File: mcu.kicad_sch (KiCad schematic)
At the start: 45 parts, among them J201 DISP, J202 SWD, J203 SPI, J204 USB serial, Q201 2N7002, SW201 Reset, U201 STM32F103CBT6, U202 USBLC6-2SC6, U203 AMS1117-3.3, Y201 8MHz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

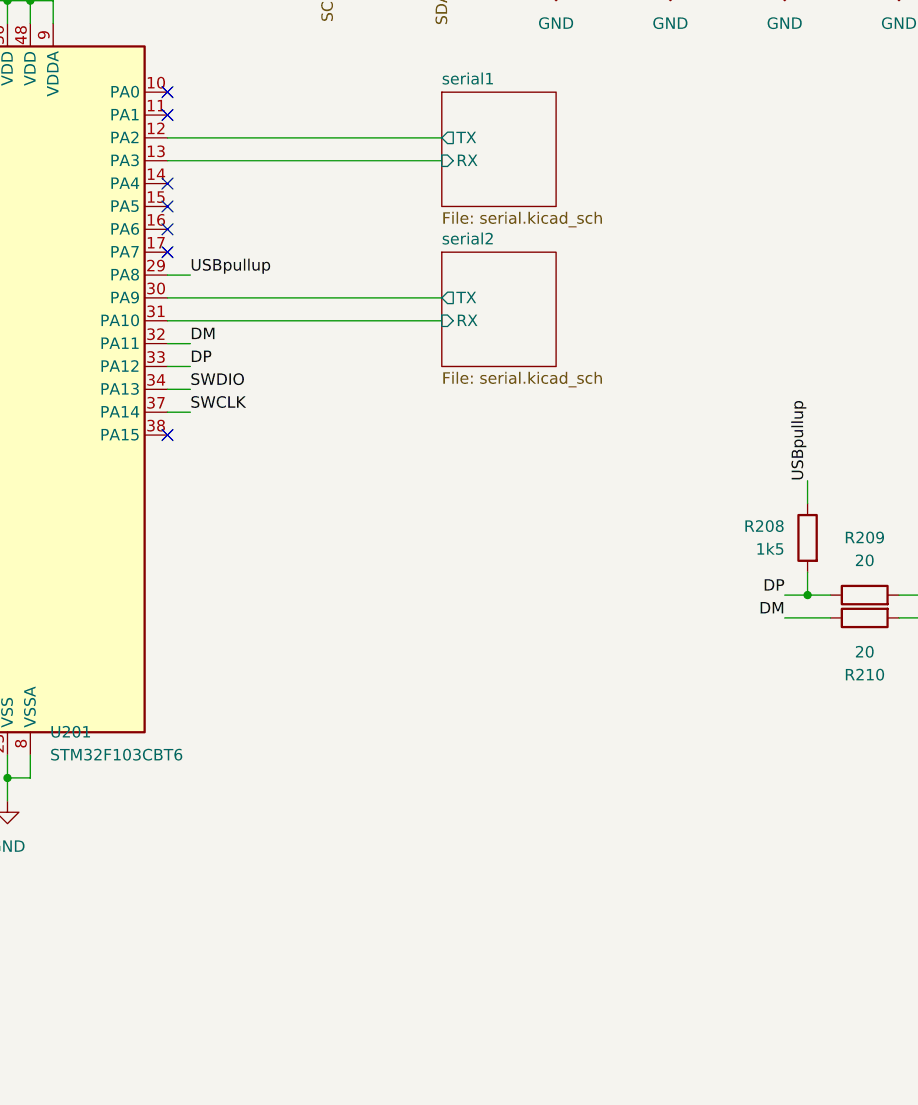
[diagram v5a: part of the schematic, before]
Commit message: Add MCU LEDs
Signed-off-by: Benedikt Spranger <b.spranger@linutronix.de>
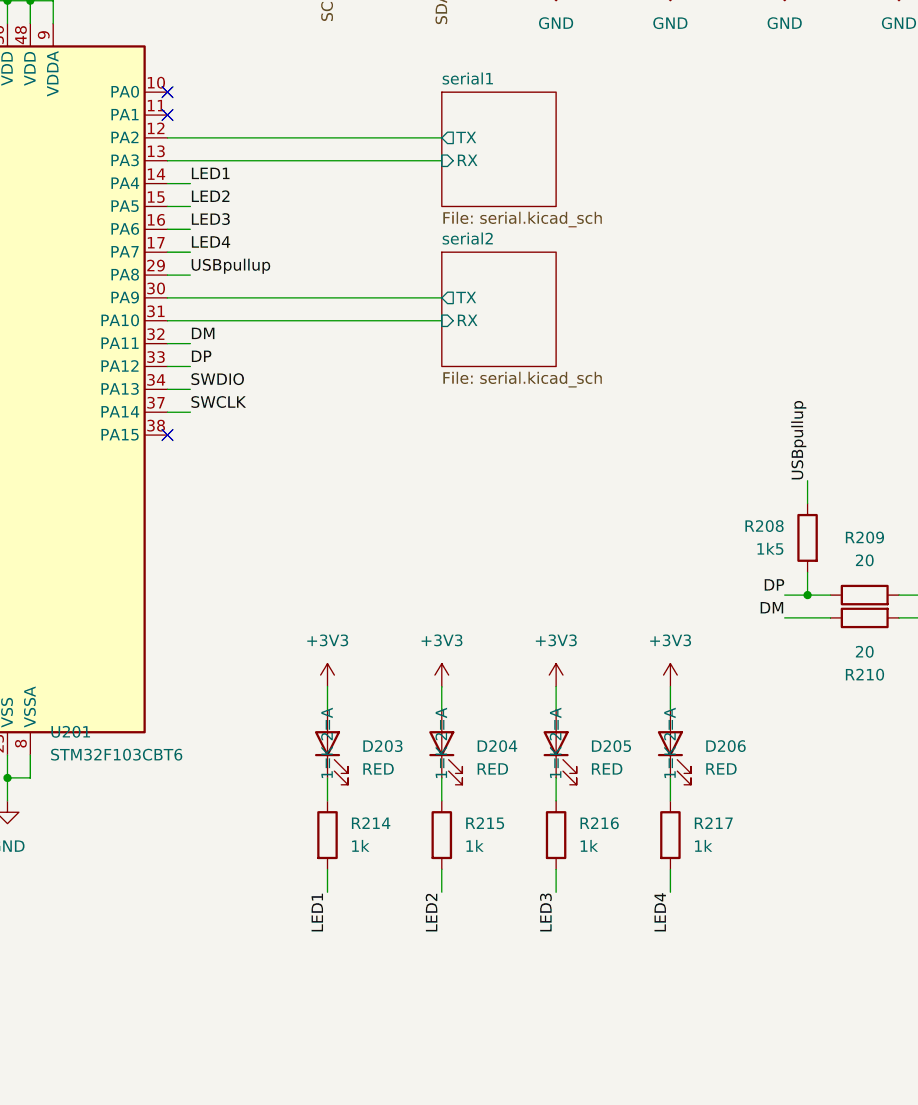
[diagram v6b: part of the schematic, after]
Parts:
- added D203, D204, D205, D206: RED, LED_SMD:LED_0603_1608Metric, symbol Device:LED
- added R214, R215, R216, R217: 1k, Resistor_SMD:R_0402_1005Metric, symbol Device:R
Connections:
- net +3V3: now also D203.2 (A), D204.2 (A), D205.2 (A), D206.2 (A)
- net LED1: now reaches U201.14 (PA4)
- net LED1: now also R214.2
- net LED2: now reaches U201.15 (PA5)
- net LED2: now also R215.2
- net LED3: now reaches U201.16 (PA6)
- net LED3: now also R216.2
- net LED4: now reaches U201.17 (PA7)
- net LED4: now also R217.2
- new net: D204.1 (K), R215.1
- new net: D205.1 (K), R216.1
- new net: D203.1 (K), R214.1
- new net: D206.1 (K), R217.1
- no-connect marks 13 -> 9

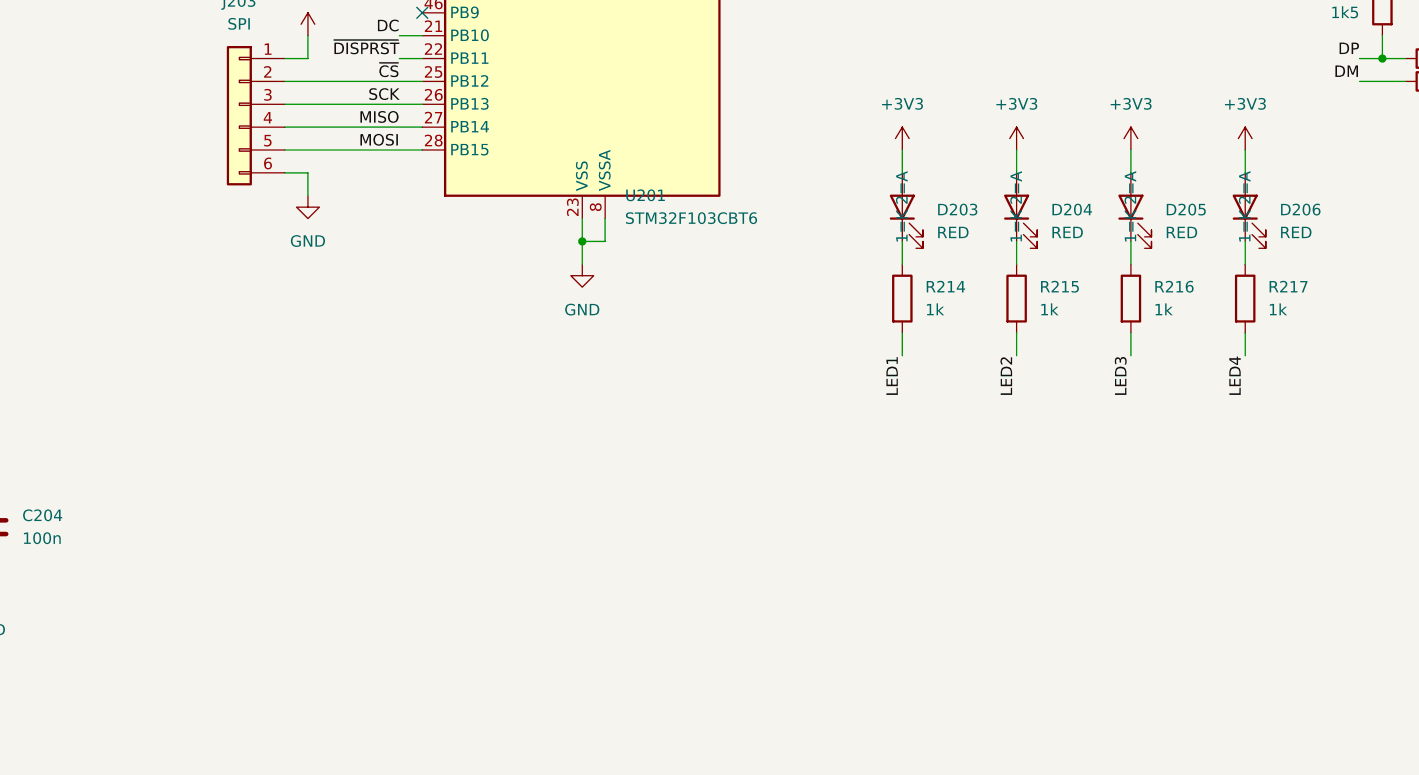
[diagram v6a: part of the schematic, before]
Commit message: Enable external I2C programming
Signed-off-by: Benedikt Spranger <b.spranger@linutronix.de>
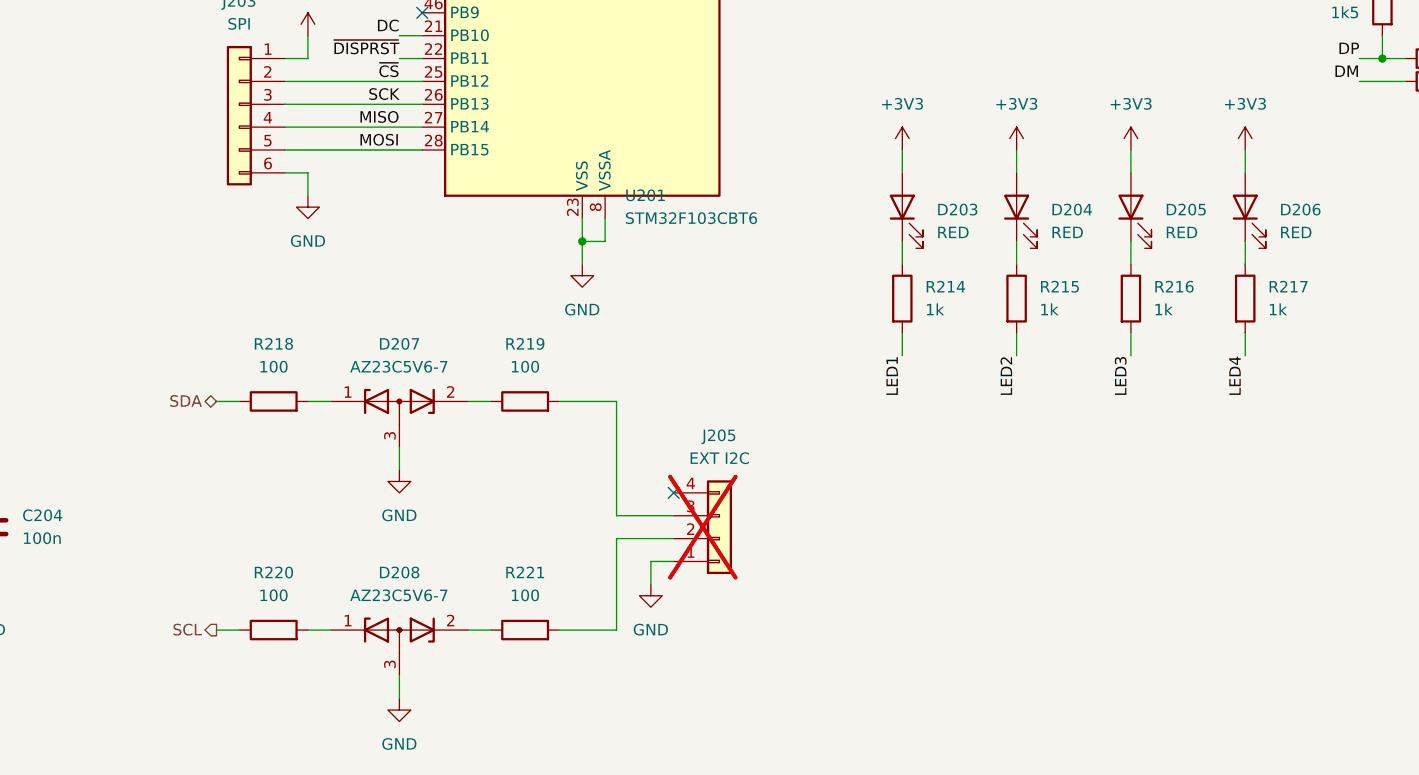
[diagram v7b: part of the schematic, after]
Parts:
- added D207, D208: AZ23C5V6-7, Package_TO_SOT_SMD:SOT-23, symbol Device:D_Zener_Dual_CommonAnode_KKA
- added J205: EXT I2C, Connector_Molex:Molex_KK-254_AE-6410-04A_1x04_P2.54mm_Vertical, symbol Connector_Generic:Conn_01x04
- added R218, R219, R220, R221: 100, Resistor_SMD:R_0402_1005Metric, symbol Device:R
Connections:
- net GND: now also D207.3 (A), D208.3 (A), J205.1 (Pin_1)
- net SCL: now also R220.1
- net SDA: now also R218.1
- new net: D207.2 (K), R219.1
- new net: J205.3 (Pin_3), R219.2
- new net: D208.1 (K), R220.2
- new net: D208.2 (K), R221.1
- new net: J205.2 (Pin_2), R221.2
- new net: D207.1 (K), R218.2
- no-connect marks 9 -> 10

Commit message: Available Parts
Signed-off-by: Benedikt Spranger <bene@eurovibes.org>
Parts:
- D203, D204, D205, D206: Long Description 90mcd Red 615nm~630nm Upright, surface-mount Red 120° 75mW 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 -> -40℃~+85℃ Red 0603 LED Indication - Discrete ROHS; MF XINGLIGHT -> Hubei KENTO Elec; MP XL-1608VRC-06 -> KT-0603R; SupplLink https://jlcpcb.com/partdetail/Xinglight-XL_1608VRC06/C73719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 -> https://jlcpcb.com/partdetail/Hubei_KentoElec-KT0603R/C2286; lcsc# C7371906 -> C2286
- R202, R204, R212: Long Description 62.5mW Thick Film Resistors 50V ±100ppm/℃ ±1% 4.7kΩ 0402 Ch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 -> 62.5mW Thick Film Resistors 50V ±100ppm/℃ ±1% 1MΩ 0402 Chip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; MP 0402WGF4701TCE -> 0402WGF1004TCE; SupplLink https://jlcpcb.com/partdetail/26643-0402WGF4701TCE/C25900 -> https://jlcpcb.com/partdetail/26826-0402WGF1004TCE/C26083; lcsc# C25900 -> C26083
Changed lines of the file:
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@@
 			)
 		)
-		(property "lcsc#" "C7371906"
+		(property "lcsc#" "C2286"
 			(at 165.1 135.89 0)
 			(effects
@@
 			)
 		)
-		(property "Long Description" "90mcd Red 615nm~630nm Upright, surface-mount Red 120° 75mW 0603 Light Emitting Diodes (LED) ROHS"
+		(property "Long Description" "-40℃~+85℃ Red 0603 LED Indication - Discrete ROHS"
 			(at 165.1 135.89 0)
 			(effects
@@
 			)
 		)
-		(property "SupplLink" "https://jlcpcb.com/partdetail/Xinglight-XL_1608VRC06/C7371906"
+		(property "SupplLink" "https://jlcpcb.com/partdetail/Hubei_KentoElec-KT0603R/C2286"
 			(at 165.1 135.89 0)
 			(effects
@@
 			)
 		)
-		(property "MF" "XINGLIGHT"
+		(property "MF" "Hubei KENTO Elec"
 			(at 165.1 135.89 0)
 			(effects
@@
 			)
 		)
-		(property "MP" "XL-1608VRC-06"
+		(property "MP" " KT-0603R"
 			(at 165.1 135.89 0)
 			(effects
@@
 			)
 		)
-		(property "lcsc#" "C7371906"
+		(property "lcsc#" "C2286"
 			(at 177.8 135.89 0)
 			(effects
@@
 			)
 		)
-		(property "Long Description" "90mcd Red 615nm~630nm Upright, surface-mount Red 120° 75mW 0603 Light Emitting Diodes (LED) ROHS"
+		(property "Long Description" "-40℃~+85℃ Red 0603 LED Indication - Discrete ROHS"
 			(at 177.8 135.89 0)
 			(effects
@@
 			)
 		)
-		(property "SupplLink" "https://jlcpcb.com/partdetail/Xinglight-XL_1608VRC06/C7371906"
+		(property "SupplLink" "https://jlcpcb.com/partdetail/Hubei_KentoElec-KT0603R/C2286"
 			(at 177.8 135.89 0)
 			(effects
@@
 			)
 		)
-		(property "MF" "XINGLIGHT"
+		(property "MF" "Hubei KENTO Elec"
 			(at 177.8 135.89 0)
 			(effects
@@
 			)
 		)
-		(property "MP" "XL-1608VRC-06"
+		(property "MP" " KT-0603R"
 			(at 177.8 135.89 0)
 			(effects
@@
 			)
 		)
-		(property "SupplLink" "https://jlcpcb.com/partdetail/26643-0402WGF4701TCE/C25900"
+		(property "SupplLink" "https://jlcpcb.com/partdetail/26826-0402WGF1004TCE/C26083"
 			(at 86.36 85.09 0)
 			(effects
@@
 			)
 		)
-		(property "Long Description" "62.5mW Thick Film Resistors 50V ±100ppm/℃ ±1% 4.7kΩ 0402 Chip Resistor - Surface Mount ROHS"
+		(property "Long Description" "62.5mW Thick Film Resistors 50V ±100ppm/℃ ±1% 1MΩ 0402 Chip Resistor - Surface Mount ROHS"
 			(at 86.36 85.09 0)
 			(effects
@@
 			)
 		)
-		(property "MP" "0402WGF4701TCE"
+		(property "MP" "0402WGF1004TCE"
 			(at 86.36 85.09 0)
 			(effects
@@
 			)
 		)
-		(property "lcsc#" "C25900"
+		(property "lcsc#" "C26083"
 			(at 86.36 85.09 0)
 			(effects
@@
 			)
 		)
-		(property "SupplLink" "https://jlcpcb.com/partdetail/26643-0402WGF4701TCE/C25900"
+		(property "SupplLink" "https://jlcpcb.com/partdetail/26826-0402WGF1004TCE/C26083"
 			(at 53.34 74.93 0)
 			(effects
@@
 			)
 		)
-		(property "Long Description" "62.5mW Thick Film Resistors 50V ±100ppm/℃ ±1% 4.7kΩ 0402 Chip Resistor - Surface Mount ROHS"
+		(property "Long Description" "62.5mW Thick Film Resistors 50V ±100ppm/℃ ±1% 1MΩ 0402 Chip Resistor - Surface Mount ROHS"
 			(at 53.34 74.93 0)
 			(effects
@@
 			)
 		)
-		(property "MP" "0402WGF4701TCE"
+		(property "MP" "0402WGF1004TCE"
 			(at 53.34 74.93 0)
 			(effects
@@
 			)
 		)
-		(property "lcsc#" "C25900"
+		(property "lcsc#" "C26083"
 			(at 53.34 74.93 0)
 			(effects
@@
 			)
 		)
-		(property "lcsc#" "C7371906"
+		(property "lcsc#" "C2286"
 			(at 152.4 135.89 0)
 			(effects
@@
 			)
 		)
-		(property "Long Description" "90mcd Red 615nm~630nm Upright, surface-mount Red 120° 75mW 0603 Light Emitting Diodes (LED) ROHS"
+		(property "Long Description" "-40℃~+85℃ Red 0603 LED Indication - Discrete ROHS"
 			(at 152.4 135.89 0)
 			(effects
@@
 			)
 		)
-		(property "SupplLink" "https://jlcpcb.com/partdetail/Xinglight-XL_1608VRC06/C7371906"
+		(property "SupplLink" "https://jlcpcb.com/partdetail/Hubei_KentoElec-KT0603R/C2286"
 			(at 152.4 135.89 0)
 			(effects
@@
 			)
 		)
-		(property "MF" "XINGLIGHT"
+		(property "MF" "Hubei KENTO Elec"
 			(at 152.4 135.89 0)
 			(effects
@@
 			)
 		)
-		(property "MP" "XL-1608VRC-06"
+		(property "MP" " KT-0603R"
 			(at 152.4 135.89 0)
 			(effects
@@
 			)
 		)
-		(property "Long Description" "62.5mW Thick Film Resistors 50V ±100ppm/℃ ±1% 4.7kΩ 0402 Chip Resistor - Surface Mount ROHS"
+		(property "Long Description" "62.5mW Thick Film Resistors 50V ±100ppm/℃ ±1% 1MΩ 0402 Chip Resistor - Surface Mount ROHS"
 			(at 254 97.79 0)
 			(effects
@@
 			)
 		)
-		(property "MP" "0402WGF4701TCE"
+		(property "MP" "0402WGF1004TCE"
 			(at 254 97.79 0)
 			(effects
@@
 			)
 		)
-		(property "SupplLink" "https://jlcpcb.com/partdetail/26643-0402WGF4701TCE/C25900"
+		(property "SupplLink" "https://jlcpcb.com/partdetail/26826-0402WGF1004TCE/C26083"
 			(at 254 97.79 0)
 			(effects
@@
 			)
 		)
-		(property "lcsc#" "C25900"
+		(property "lcsc#" "C26083"
 			(at 254 97.79 0)
 			(effects
@@
 			)
 		)
-		(property "lcsc#" "C7371906"
+		(property "lcsc#" "C2286"
 			(at 190.5 135.89 0)
 			(effects
@@
 			)
 		)
-		(property "Long Description" "90mcd Red 615nm~630nm Upright, surface-mount Red 120° 75mW 0603 Light Emitting Diodes (LED) ROHS"
+		(property "Long Description" "-40℃~+85℃ Red 0603 LED Indication - Discrete ROHS"
 			(at 190.5 135.89 0)
 			(effects
@@
 			)
 		)
-		(property "SupplLink" "https://jlcpcb.com/partdetail/Xinglight-XL_1608VRC06/C7371906"
+		(property "SupplLink" "https://jlcpcb.com/partdetail/Hubei_KentoElec-KT0603R/C2286"
 			(at 190.5 135.89 0)
 			(effects
@@
 			)
 		)
-		(property "MF" "XINGLIGHT"
+		(property "MF" "Hubei KENTO Elec"
 			(at 190.5 135.89 0)
 			(effects
@@
 			)
 		)
-		(property "MP" "XL-1608VRC-06"
+		(property "MP" " KT-0603R"
 			(at 190.5 135.89 0)
 			(effects
